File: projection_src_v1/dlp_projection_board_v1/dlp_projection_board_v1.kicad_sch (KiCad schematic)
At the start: 0 parts

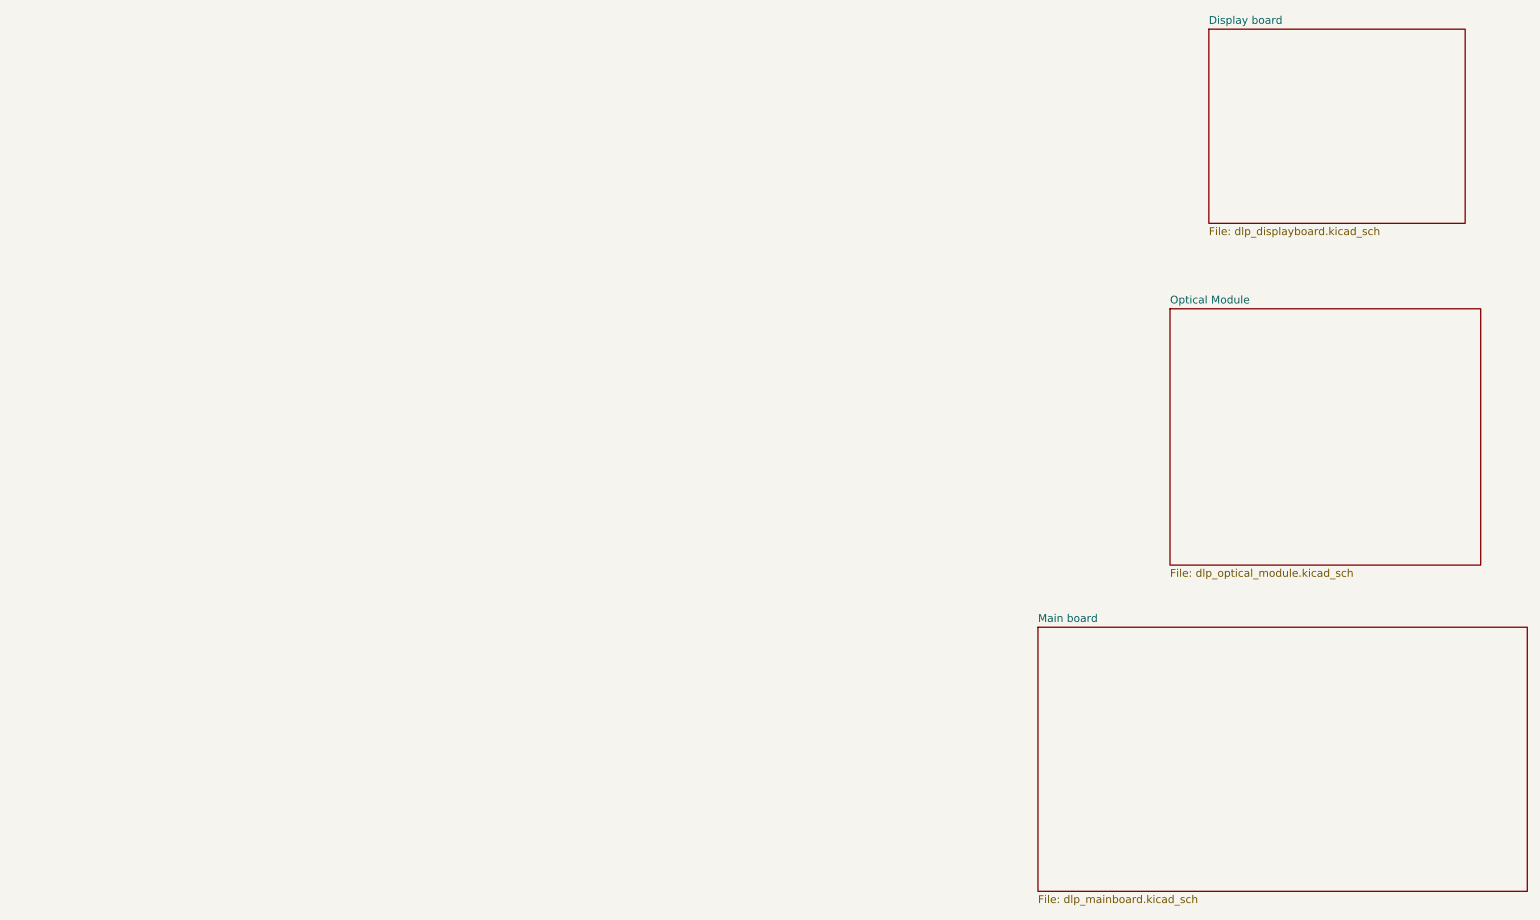
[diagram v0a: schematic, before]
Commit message: Added schematic template
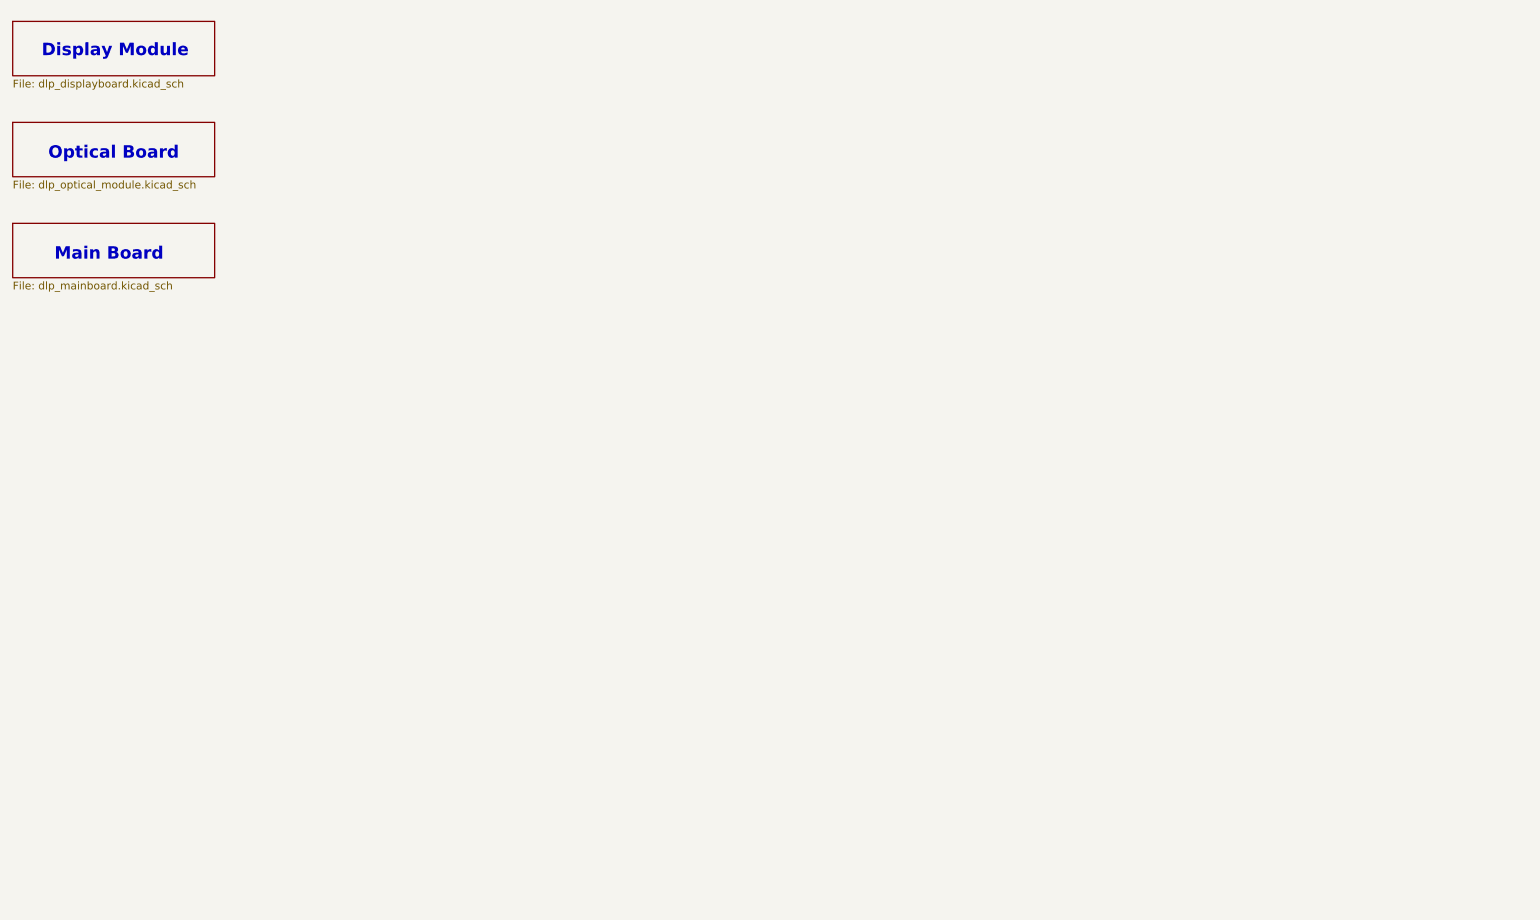
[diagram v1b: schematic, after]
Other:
- note added: "Display Module"
- note added: "Main Board"
- note added: "Optical Board"
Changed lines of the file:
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@@
 	(generator "eeschema")
 	(generator_version "8.0")
-	(paper "A4")
+	(paper "A5")
+	(title_block
+		(date "2024-11-15")
+	)
+	(text "Optical Board\n"
+		(exclude_from_sim no)
+		(at 38.1 40.64 0)
+		(effects
+			(font
+				(size 2.032 2.032)
+				(thickness 0.4064)
+				(bold yes)
+			)
+		)
+	)
+	(text "Main Board"
+		(exclude_from_sim no)
+		(at 37.338 57.15 0)
+		(effects
+			(font
+				(size 2.032 2.032)
+				(thickness 0.4064)
+				(bold yes)
+			)
+		)
+	)
+	(text "Display Module"
+		(exclude_from_sim no)
+		(at 38.354 23.876 0)
+		(effects
+			(font
+				(size 2.032 2.032)
+				(thickness 0.4064)
+				(bold yes)
+			)
+		)
+	)
 	(sheet
-		(at 189.23 118.11)
-		(size 80.01 43.18)
+		(at 21.59 52.07)
+		(size 33.02 8.89)
 		(fields_autoplaced yes)
 		(stroke
@@
 		)
 		(property "Sheetname" "Main board"
-			(at 189.23 117.3984 0)
+			(at 21.59 51.3584 0)
 			(show_name yes)
 			(effects
@@
 				)
 				(justify left bottom)
+				(hide yes)
 			)
 		)
 		(property "Sheetfile" "dlp_mainboard.kicad_sch"
-			(at 189.23 161.8746 0)
+			(at 21.59 61.5446 0)
 			(effects
 				(font
@@
 	)
 	(sheet
-		(at 217.17 20.32)
-		(size 41.91 31.75)
+		(at 21.59 19.05)
+		(size 33.02 8.89)
 		(fields_autoplaced yes)
 		(stroke
@@
 		)
 		(property "Sheetname" "Display board"
-			(at 217.17 19.6084 0)
+			(at 21.59 18.3384 0)
 			(effects
 				(font
@@
 				)
 				(justify left bottom)
+				(hide yes)
 			)
 		)
 		(property "Sheetfile" "dlp_displayboard.kicad_sch"
-			(at 217.17 52.6546 0)
+			(at 21.59 28.5246 0)
 			(effects
 				(font
@@
 	)
 	(sheet
-		(at 210.82 66.04)
-		(size 50.8 41.91)
+		(at 21.59 35.56)
+		(size 33.02 8.89)
 		(fields_autoplaced yes)
 		(stroke
@@
 		)
 		(property "Sheetname" "Optical Module"
-			(at 210.82 65.3284 0)
+			(at 21.59 34.8484 0)
 			(effects
 				(font
@@
 				)
 				(justify left bottom)
+				(hide yes)
 			)
 		)
 		(property "Sheetfile" "dlp_optical_module.kicad_sch"
-			(at 210.82 108.5346 0)
+			(at 21.59 45.0346 0)
 			(effects
 				(font

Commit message: Added DMD, Controller and Driver symbols
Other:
- title: (none) -> Lithostepper DLP projector board
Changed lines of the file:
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@@
 	(paper "A5")
 	(title_block
+		(title "Lithostepper DLP projector board")
 		(date "2024-11-15")
 	)
